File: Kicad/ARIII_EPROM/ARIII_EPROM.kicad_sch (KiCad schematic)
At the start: 33 parts, among them CN1 ECC43DCAI-S189, Q1 ZVP2106A, Q2 ZVP2106A, SW1 SW_Push, SW2 SW_Wuerth_450301014042, U1 GAL16V8, U10 IS62C256AL, U11 MC1455B, U2 GAL16V8, U3 GAL16V8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

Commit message: Replaced footprints for U8 and U10
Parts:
- U10, U8: footprint Package_SO:SOIC-28W_7.5x18.7mm_P1.27mm -> ARIII_Shared:SOP-28_MIL330_ALL
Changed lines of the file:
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@@
 			)
 		)
-		(property "Footprint" "Package_SO:SOIC-28W_7.5x18.7mm_P1.27mm"
+		(property "Footprint" "ARIII_Shared:SOP-28_MIL330_ALL"
 			(at 275.336 149.098 0)
 			(effects
@@
 			)
 		)
-		(property "Footprint" "Package_SO:SOIC-28W_7.5x18.7mm_P1.27mm"
+		(property "Footprint" "ARIII_Shared:SOP-28_MIL330_ALL"
 			(at 340.106 150.368 0)
 			(effects

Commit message: Replaced EPROM footprints with custom footprints from a project library
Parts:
- U7, U9: footprint SamacSys_Parts:DIP1499W56P254L4188H572Q32N -> ARIII_Shared:DIP-32_W15.24mm-SmallerPads
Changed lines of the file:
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@@
 			)
 		)
-		(property "Footprint" "SamacSys_Parts:DIP1499W56P254L4188H572Q32N"
+		(property "Footprint" "ARIII_Shared:DIP-32_W15.24mm-SmallerPads"
 			(at 350.52 158.75 0)
 			(effects
@@
 			)
 		)
-		(property "Footprint" "SamacSys_Parts:DIP1499W56P254L4188H572Q32N"
+		(property "Footprint" "ARIII_Shared:DIP-32_W15.24mm-SmallerPads"
 			(at 287.02 158.75 0)
 			(effects

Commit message: Changed footprint association for U6
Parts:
- U6: footprint Package_SO:SO-14_3.9x8.65mm_P1.27mm -> ARIII_Shared:SO-14_Hyrbrid
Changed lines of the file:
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@@
 			)
 		)
-		(property "Footprint" "Package_SO:SO-14_3.9x8.65mm_P1.27mm"
+		(property "Footprint" "ARIII_Shared:SO-14_Hyrbrid"
 			(at 318.77 256.54 0)
 			(effects
@@
 			)
 		)
-		(property "Footprint" "Package_SO:SO-14_3.9x8.65mm_P1.27mm"
+		(property "Footprint" "ARIII_Shared:SO-14_Hyrbrid"
 			(at 478.79 307.34 0)
 			(effects
@@
 			)
 		)
-		(property "Footprint" "Package_SO:SO-14_3.9x8.65mm_P1.27mm"
+		(property "Footprint" "ARIII_Shared:SO-14_Hyrbrid"
 			(at 283.21 274.32 0)
 			(effects

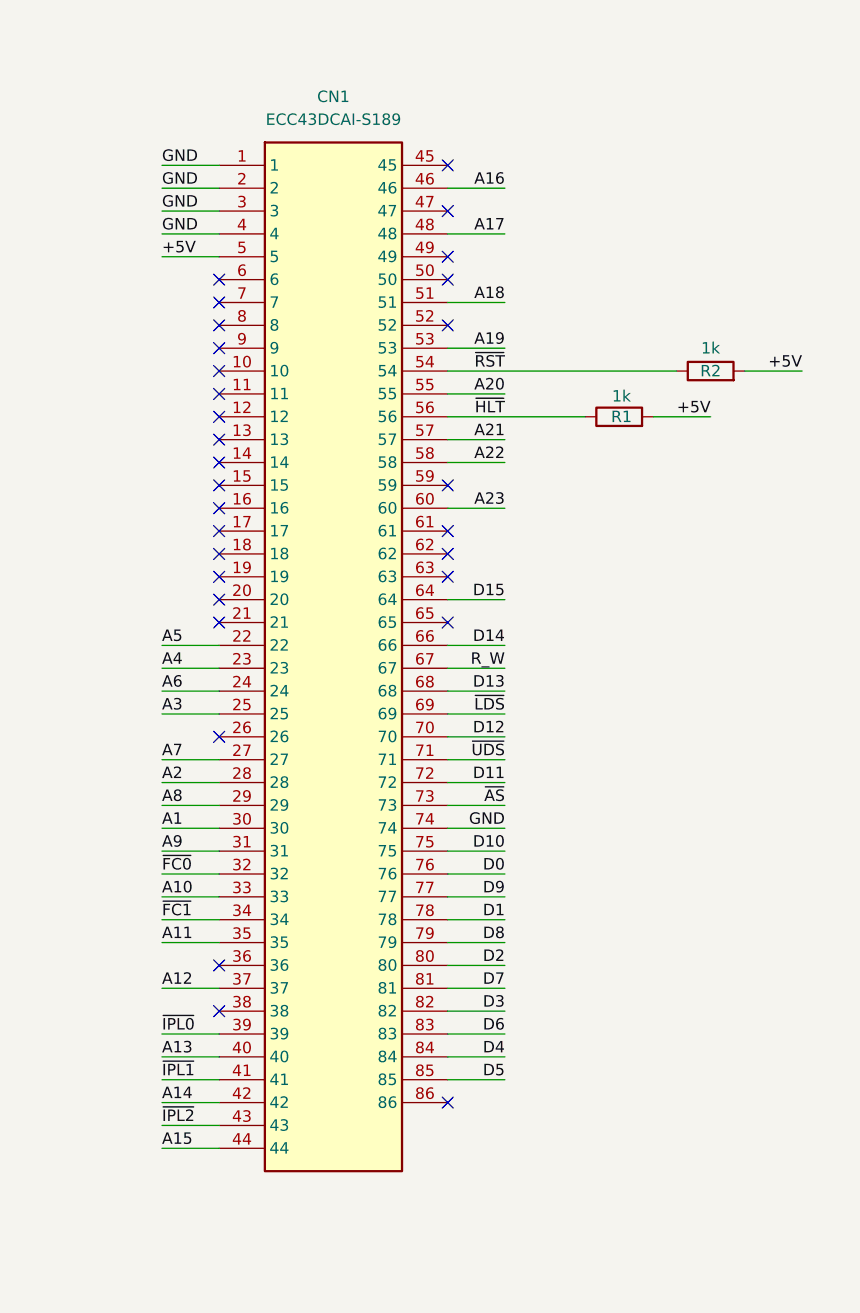
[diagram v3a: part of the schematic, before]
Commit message: fixed cn1 pin numbering
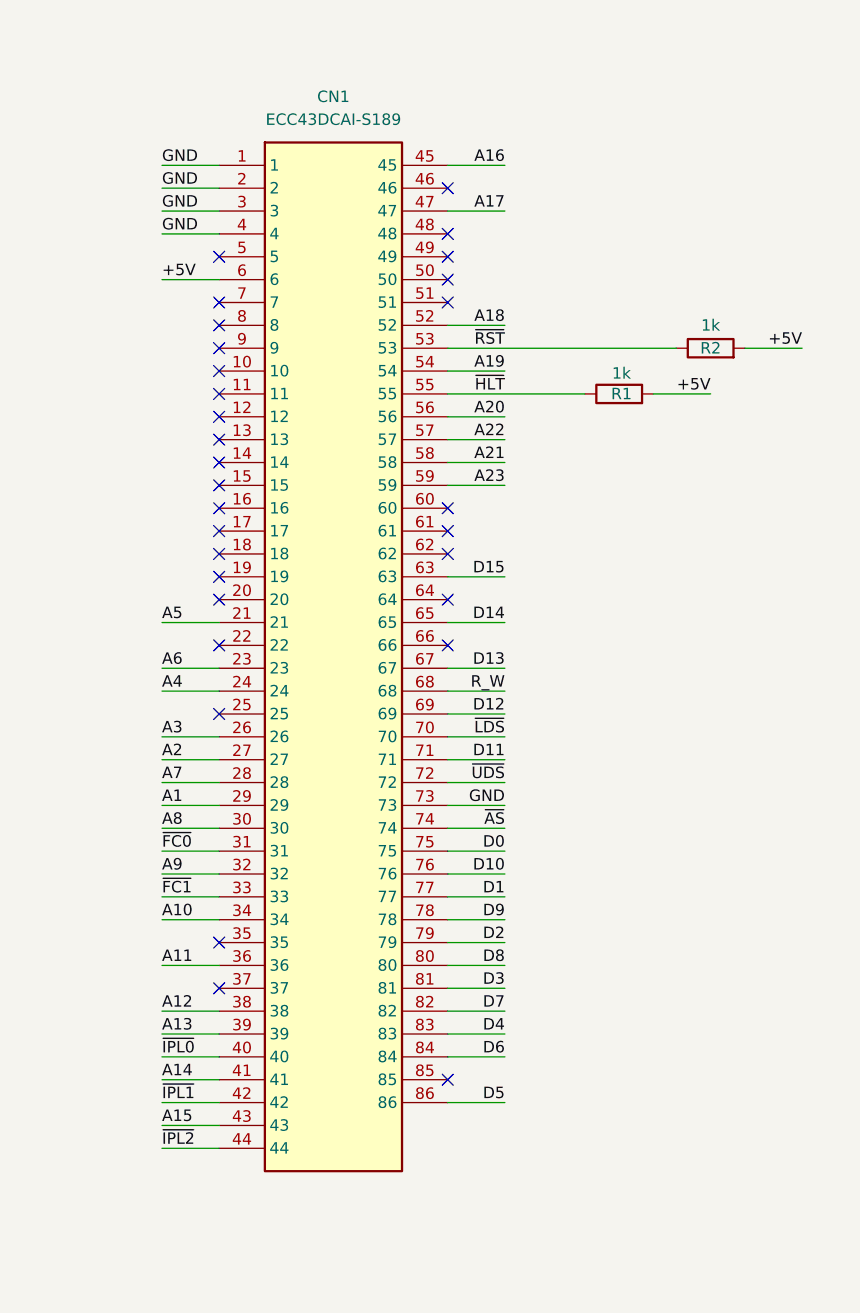
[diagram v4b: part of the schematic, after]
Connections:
- net +5V: now also CN1.6; no longer CN1.5
- net A1: now also CN1.29; no longer CN1.30
- net A10: now also CN1.34; no longer CN1.33
- net A11: now also CN1.36; no longer CN1.35
- net A12: now also CN1.38; no longer CN1.37
- net A13: now also CN1.39; no longer CN1.40
- net A14: now also CN1.41; no longer CN1.42
- net A15: now also CN1.43; no longer CN1.44
- net A16: now also CN1.45; no longer CN1.46
- net A17: now also CN1.47; no longer CN1.48
- net A18: now also CN1.52; no longer CN1.51
- net A19: now also CN1.54; no longer CN1.53
- net A2: now also CN1.27; no longer CN1.28
- net A20: now also CN1.56; no longer CN1.55
- net A21: now also CN1.58; no longer CN1.57
- net A22: now also CN1.57; no longer CN1.58
- net A23: now also CN1.59; no longer CN1.60
- net A3: now also CN1.26; no longer CN1.25
- net A4: now also CN1.24; no longer CN1.23
- net A5: now also CN1.21; no longer CN1.22
- net A6: now also CN1.23; no longer CN1.24
- net A7: now also CN1.28; no longer CN1.27
- net A8: now also CN1.30; no longer CN1.29
- net A9: now also CN1.32; no longer CN1.31
- net D0: now also CN1.75; no longer CN1.76
- net D1: now also CN1.77; no longer CN1.78
- net D10: now also CN1.76; no longer CN1.75
- net D11: now also CN1.71; no longer CN1.72
- net D12: now also CN1.69; no longer CN1.70
- net D13: now also CN1.67; no longer CN1.68
- net D14: now also CN1.65; no longer CN1.66
- net D15: now also CN1.63; no longer CN1.64
- net D2: now also CN1.79; no longer CN1.80
- net D3: now also CN1.81; no longer CN1.82
- net D4: now also CN1.83; no longer CN1.84
- net D5: now also CN1.86; no longer CN1.85
- net D6: now also CN1.84; no longer CN1.83
- net D7: now also CN1.82; no longer CN1.81
- net D8: now also CN1.80; no longer CN1.79
- net D9: now also CN1.78; no longer CN1.77
- net GND: now also CN1.73; no longer CN1.74
- net R_W: now also CN1.68; no longer CN1.67
- net ~{AS}: now also CN1.74; no longer CN1.73
- net ~{FC0}: now also CN1.31; no longer CN1.32
- net ~{FC1}: now also CN1.33; no longer CN1.34
- net ~{HLT}: now also CN1.55; no longer CN1.56
- net ~{IPL0}: now also CN1.40; no longer CN1.39
- net ~{IPL1}: now also CN1.42; no longer CN1.41
- net ~{IPL2}: now also CN1.44; no longer CN1.43
- net ~{LDS}: now also CN1.70; no longer CN1.69
- net ~{RST}: now also CN1.53; no longer CN1.54
- net ~{UDS}: now also CN1.72; no longer CN1.71
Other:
- moved on the sheet: R1, R2
